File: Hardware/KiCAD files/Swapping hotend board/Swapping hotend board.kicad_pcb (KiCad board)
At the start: 2 copper layers, 3 parts, among them J19 PINHD_1x10_Male, J24 JST_SMD_1.0mm_Vertical

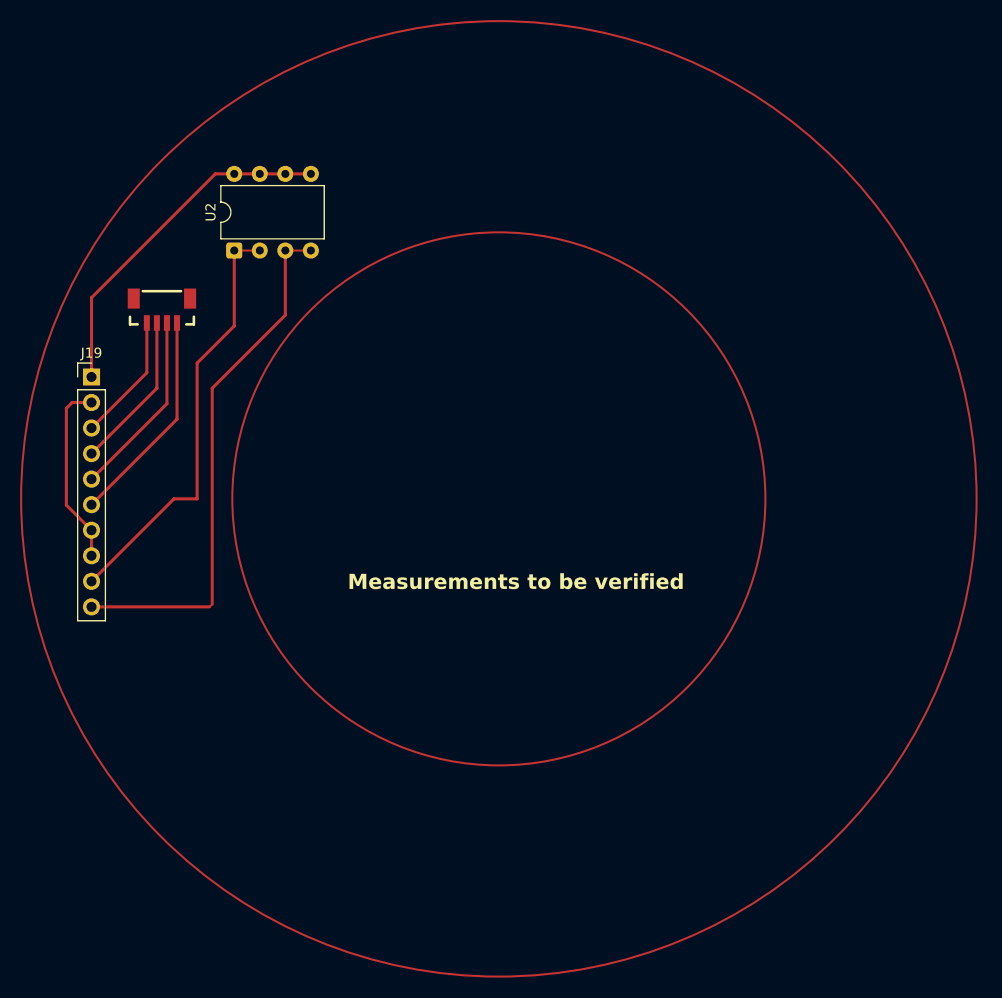
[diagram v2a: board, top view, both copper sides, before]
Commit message: general progress and adjustments
new footprint for pi reg inductor, var reg checked concurred with current part and value. re footprinted motor driver. started swapping head. adjusted some device footprints.
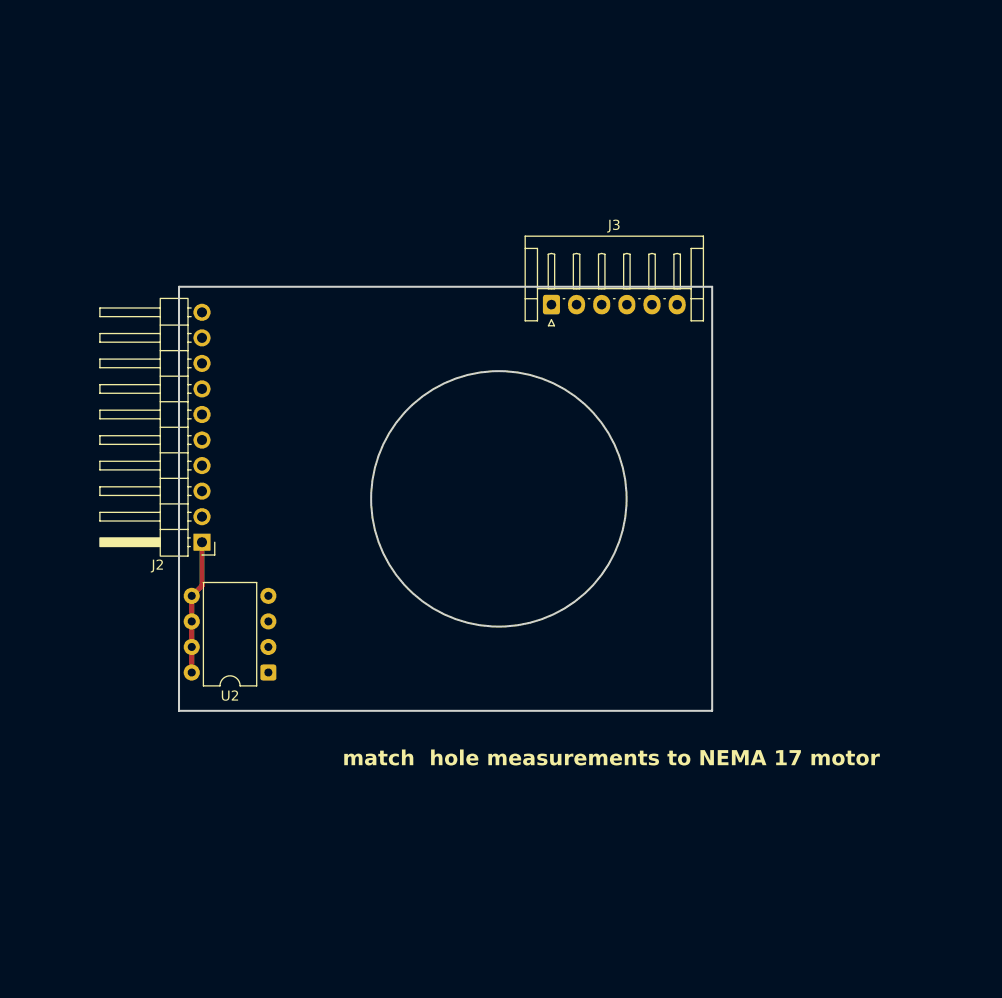
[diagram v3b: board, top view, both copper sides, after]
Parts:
- removed J19: PINHD_1x10_Male, Connector_PinHeader_2.54mm:PinHeader_1x10_P2.54mm_Vertical
- removed J24: JST_SMD_1.0mm_Vertical, PCM_SparkFun-Connector:JST_1x04_P1.0mm_Vertical_SMD
- added J2: PINHD_1x10_Male, Connector_PinHeader_2.54mm:PinHeader_1x10_P2.54mm_Horizontal, F.Cu at (57.4, 107.4)
- added J3: JST_06, Connector_JST:JST_EH_S6B-EH_1x06_P2.50mm_Horizontal, F.Cu at (92.1, 83.8)
- moved U2 42.1 mm to (64.0, 120.4), turned to 180 degrees
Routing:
- net Net-(U2-SW2-P1): track 52.8 -> 0.00 mm
- net Net-(U2-SW1-P1): track 42.7 -> 0.00 mm
- net Net-(U2-SW1-P1-input): track 35.3 -> 13.4 mm
- net Net-(J24-Pin_4): track 21.6 -> 0.00 mm
- net Net-(J24-Pin_3): track 18.6 -> 0.00 mm
- net GND: track 18.4 -> 0.00 mm
- net Net-(J24-Pin_2): track 15.7 -> 0.00 mm
- net Net-(J24-Pin_1): track 12.7 -> 0.00 mm
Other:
- board outline added: 53 x 42.2 mm
- board text added: "match hole measurements to NEMA 17 motor"
- board text removed: "Measurements to be verified"

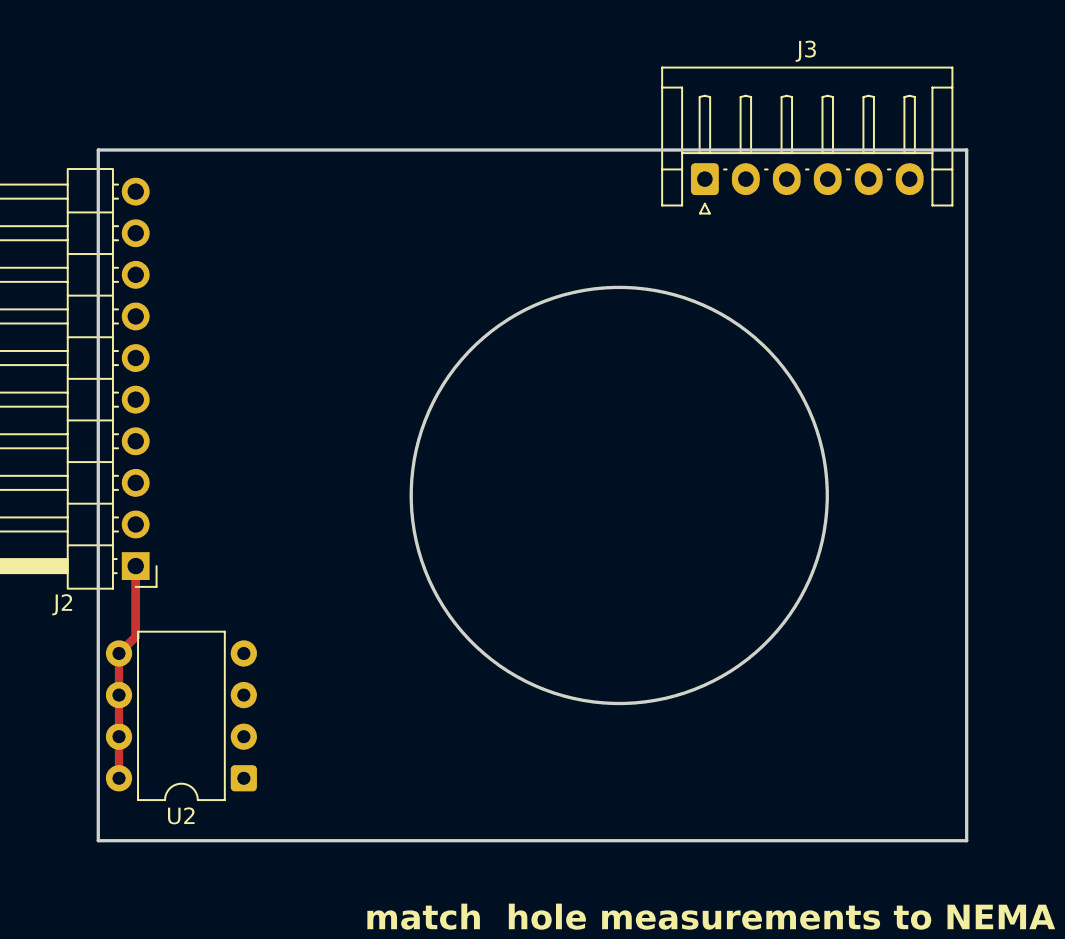
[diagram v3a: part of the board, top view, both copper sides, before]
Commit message: DRV 8825 and regulator purchased set
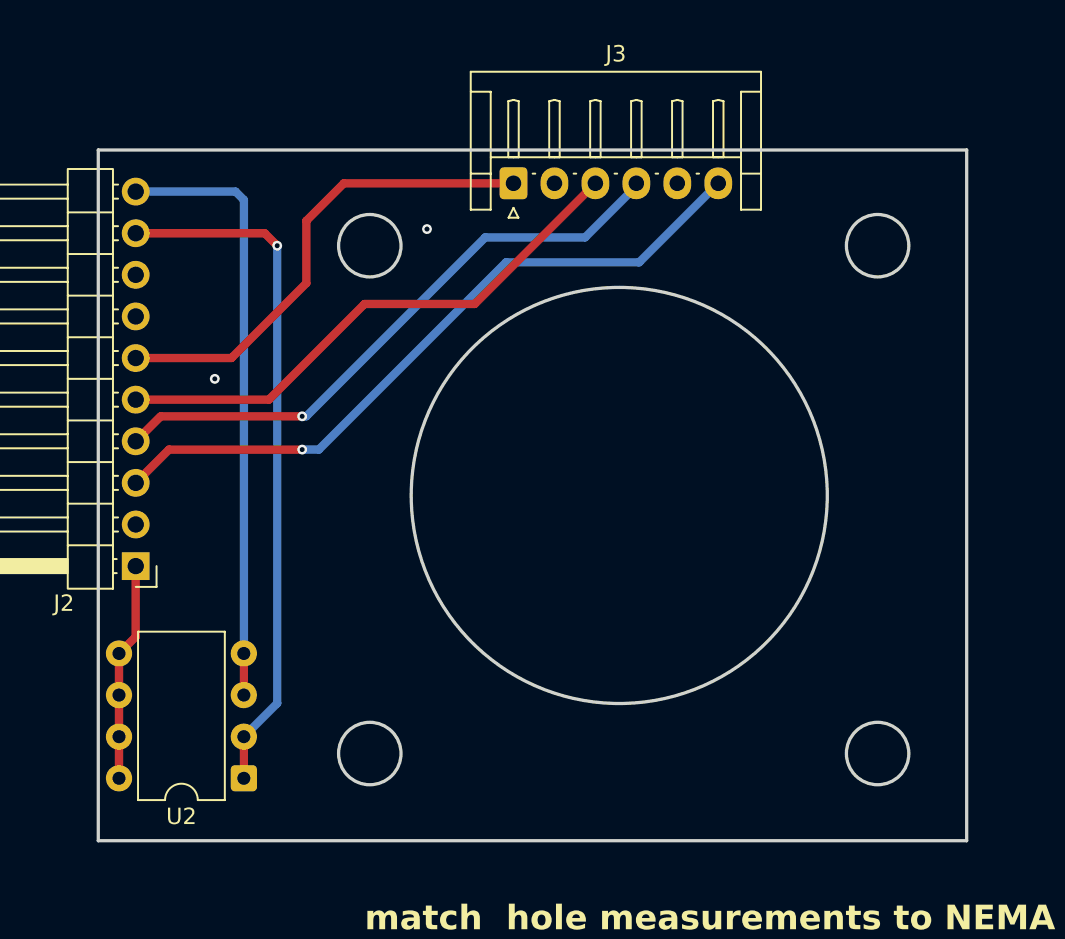
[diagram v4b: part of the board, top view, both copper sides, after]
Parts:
- moved J3 11.7 mm to (80.5, 84.1)
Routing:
- net /B2: track 0.00 -> 43.1 mm, vias 0 -> 1
- net Net-(U2-SW1-P1): track 0.00 -> 42.3 mm, vias 0 -> 1
- net /A2: track 0.00 -> 37.2 mm, vias 0 -> 1
- net Net-(U2-SW2-P1): track 0.00 -> 37.0 mm
- net /B1: track 0.00 -> 33.7 mm
- net /A1: track 0.00 -> 30.3 mm
- net GND: vias 0 -> 2
- added copper zone on B.Cu, net GND
- added copper zone on F.Cu, net GND
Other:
- outline, holes or cut-outs redrawn

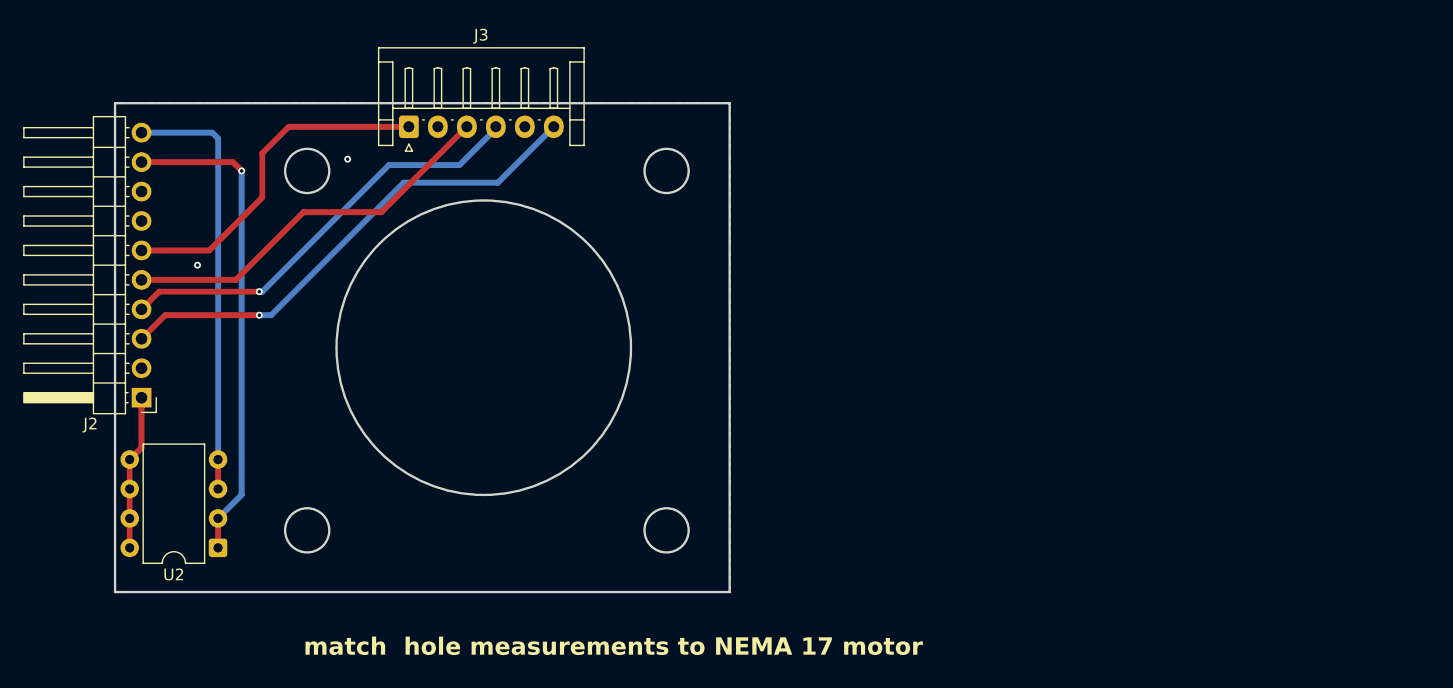
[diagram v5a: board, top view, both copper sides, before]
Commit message: Compatability mods
basic modifications to work toward compatability between boards physically on the hotend
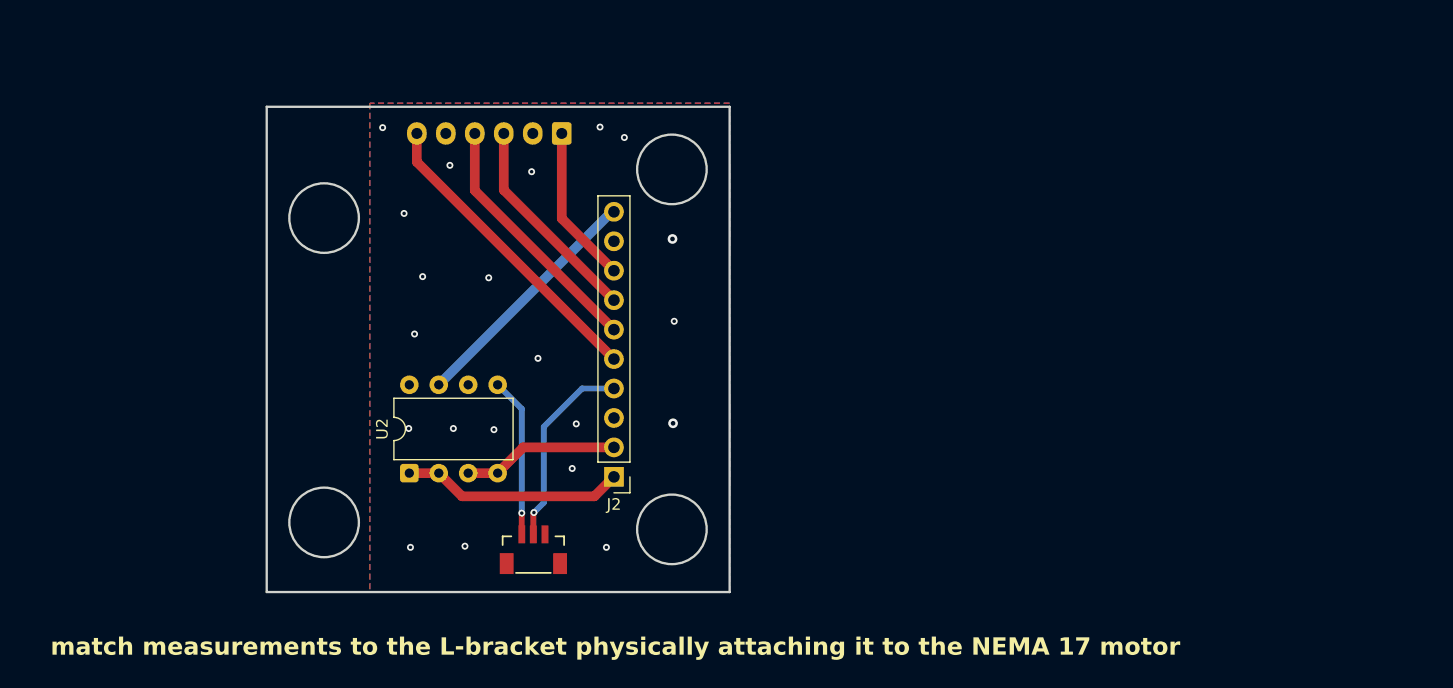
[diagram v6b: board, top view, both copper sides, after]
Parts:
- added J18: JST_1mm_3_Vertical, PCM_SparkFun-Connector:JST_1x03_P1.0mm_Vertical_SMD, F.Cu at (91.2, 122.7)
- J2: footprint Connector_PinHeader_2.54mm:PinHeader_1x10_P2.54mm_Horizontal -> Connector_PinHeader_2.54mm:PinHeader_1x10_P2.54mm_Vertical
- J3: moved to B.Cu
- moved J2 41.3 mm to (98.2, 114.3)
- moved U2 17.7 mm to (80.5, 114.0), turned to 90 degrees
- moved J3 13.2 mm to (93.7, 84.7), turned to 180 degrees
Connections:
- J2 pad 1: Net-(U2-SW1-P1-input) -> Net-(U2-SW1-P1)
- J2 pad 10: Net-(U2-SW2-P1) -> Net-(U2-SW1-P1-input)
- J2 pad 2: GND -> Net-(U2-SW2-P1)
- J2 pad 3: /B2 -> GND
- J2 pad 4: /A2 -> Net-(J18-Pad2)
- J2 pad 5: /B1 -> /B2
- J2 pad 6: /A1 -> /A2
- J2 pad 7: GND -> /B1
- J2 pad 8: GND -> /A1
- J2 pad 9: Net-(U2-SW1-P1) -> GND
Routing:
- net Net-(U2-SW2-P1): track 37.0 -> 13.5 mm
- net Net-(U2-SW1-P1): track 42.3 -> 19.2 mm, vias 1 -> 0
- net Net-(U2-SW1-P1-input): track 13.4 -> 35.1 mm, vias 0 -> 1
- net Net-(J18-Pad2): track 0.00 -> 17.1 mm, vias 0 -> 1
- net /B2: track 43.1 -> 26.5 mm, vias 1 -> 0
- net /A1: track 30.3 -> 13.7 mm
- net /B1: track 33.7 -> 18.3 mm
- net /A2: track 37.2 -> 21.9 mm, vias 1 -> 0
- net GND: vias 2 -> 21
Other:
- board size 53 x 42.2 mm -> 39.9 x 41.9 mm
- board text added: "match measurements to the L-bracket physically attaching it to the NEMA 17 motor"
- board text removed: "match hole measurements to NEMA 17 motor"

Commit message: approved with final adjustments
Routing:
- net GND: vias 21 -> 23
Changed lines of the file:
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@@
+		(layer "User.1")
+		(pts
+			(xy 103.15 118.8) (xy 103.15 87.75)
+		)
+		(height 11.5)
+		(orientation 1)
+		(format
+			(prefix "")
+			(suffix "")
+			(units 3)
+			(units_format 0)
+			(precision 4)
+			(suppress_zeroes yes)
+		)
+		(style
+			(thickness 0.2)
+			(arrow_length 1.27)
+			(text_position_mode 0)
+			(arrow_direction outward)
+			(extension_height 0.58642)
+			(extension_offset 0.5)
+			(keep_text_aligned yes)
+		)
+		(gr_text "31.05"
+			(at 112.85 103.275 90)
+			(layer "User.1")
+			(effects
+				(font
+					(size 1.5 1.5)
+					(thickness 0.3)
+				)
+			)
+		)
+	)
+	(dimension
+		(type orthogonal)
 		(layer "User.1")
 		(pts
@@
 	)
 	(via
+		(at 97 87.9)
+		(size 0.6)
+		(drill 0.3)
+		(layers "F.Cu" "B.Cu")
+		(free yes)
+		(net "GND")
+	)
+	(via
 		(at 103.2 93.75)
 		(size 0.8382)
@@
 	)
 	(via
+		(at 103.25 112.15)
+		(size 0.6)
+		(drill 0.3)
+		(layers "F.Cu" "B.Cu")
+		(free yes)
+		(net "GND")
+	)
+	(via
 		(at 85.3 120.25)
 		(size 0.6)
@@
 	)
 	(via
-		(at 103.25 109.65)
+		(at 103.05 106.5)
 		(size 0.8382)
 		(drill 0.4)

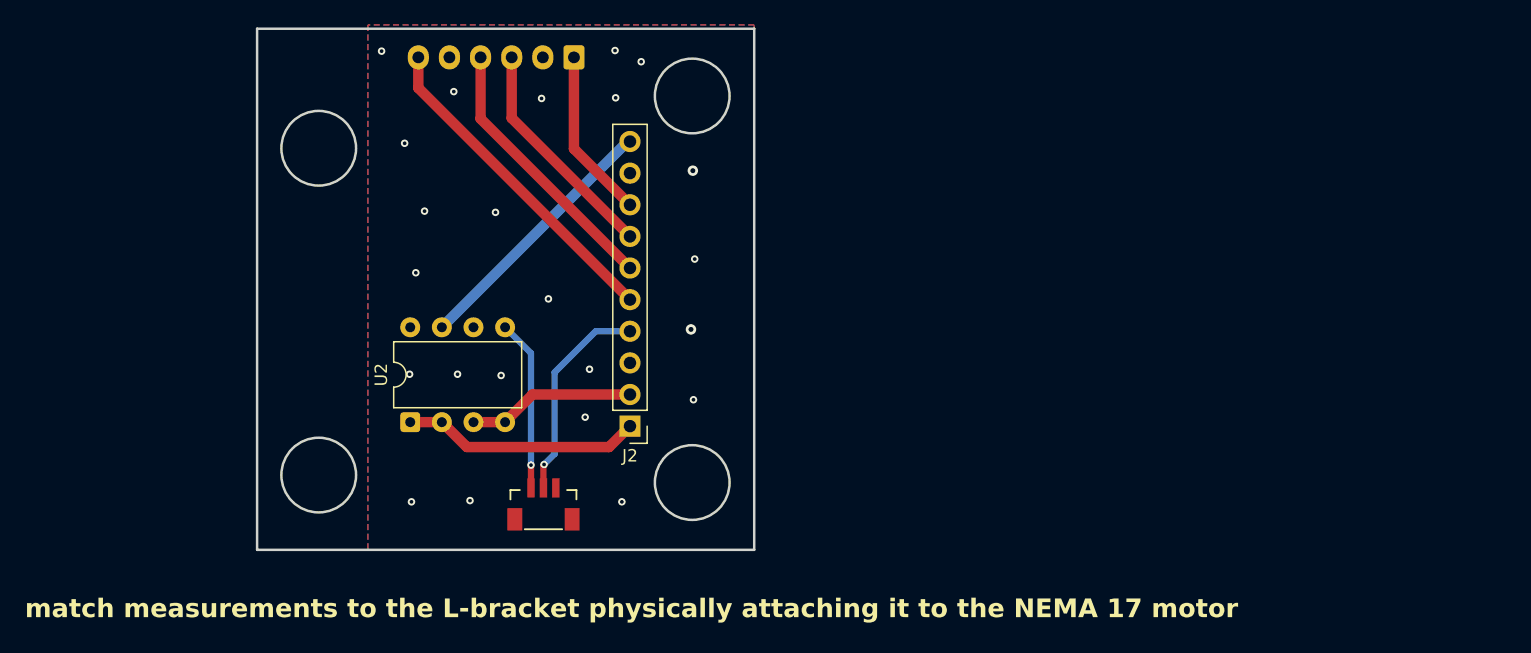
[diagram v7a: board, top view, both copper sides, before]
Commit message: V1 boards after final board invoice
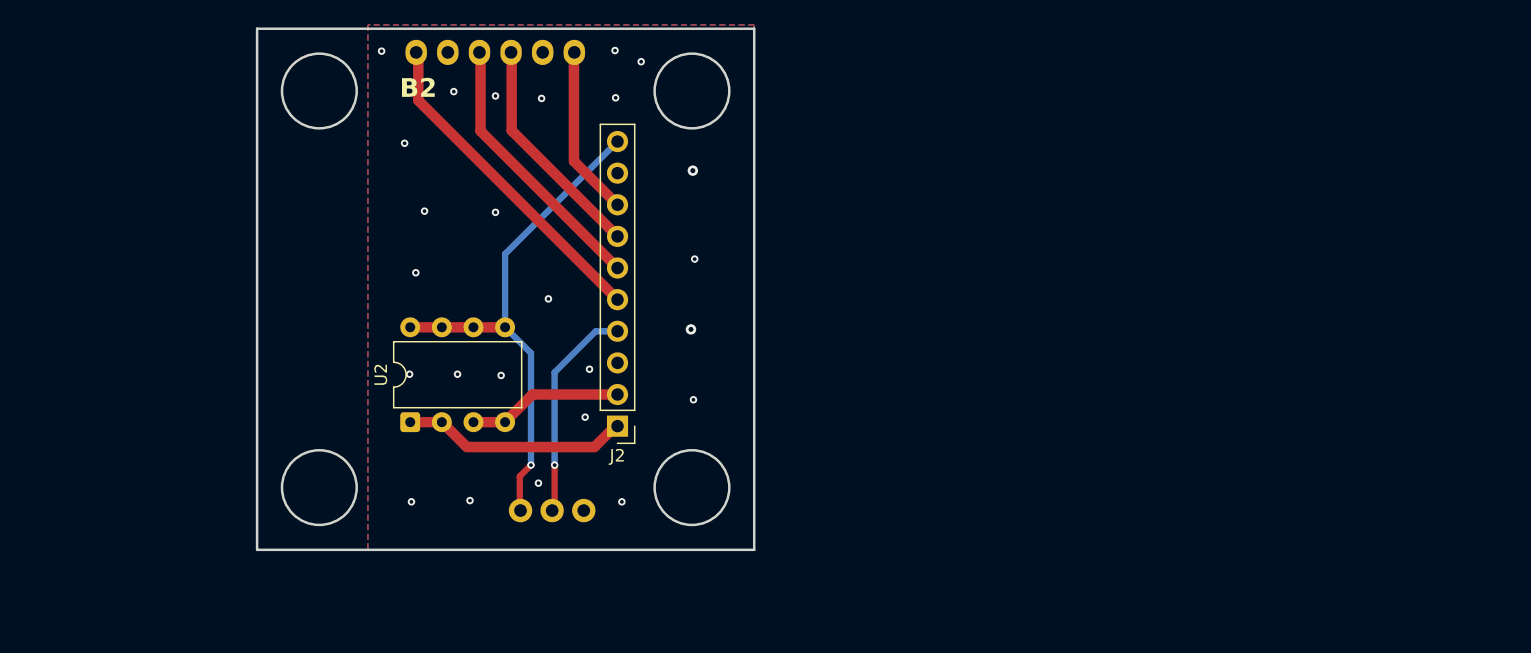
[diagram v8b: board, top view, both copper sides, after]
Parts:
- J18: footprint PCM_SparkFun-Connector:JST_1x03_P1.0mm_Vertical_SMD -> PCM_SparkFun-Connector:1x03_P2.54mm
- J3: footprint Connector_JST:JST_EH_S6B-EH_1x06_P2.50mm_Horizontal -> PCM_4ms_Connector:Pins_1x06_2.54mm_TH_SWD
- moved J3 6.33 mm to (87.3, 84.2), turned to 90 degrees
- moved J18 3.62 mm to (94.4, 121.0)
- moved J2 1.00 mm to (97.2, 114.3)
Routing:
- net Net-(U2-SW1-P1-input): track 35.1 -> 41.9 mm
- net Net-(U2-SW2-P1): track 13.5 -> 12.5 mm
- net Net-(U2-SW1-P1): track 19.2 -> 18.4 mm
- net Net-(J18-Pad2): track 17.1 -> 17.6 mm
- net GND: vias 23 -> 25
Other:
- outline, holes or cut-outs redrawn
- board text added: "B2"
